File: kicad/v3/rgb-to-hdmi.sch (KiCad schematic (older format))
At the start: 26 parts, among them P1 CONN_02X20, P2 CONN_01X03, P3 CONN_01X06, P4 CONN_01X02, P5 CONN_01X06, P6 CONN_01X02, P7 Conn_01x01, SW1 SW_PUSH, SW2 SW_PUSH, SW3 SW_PUSH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

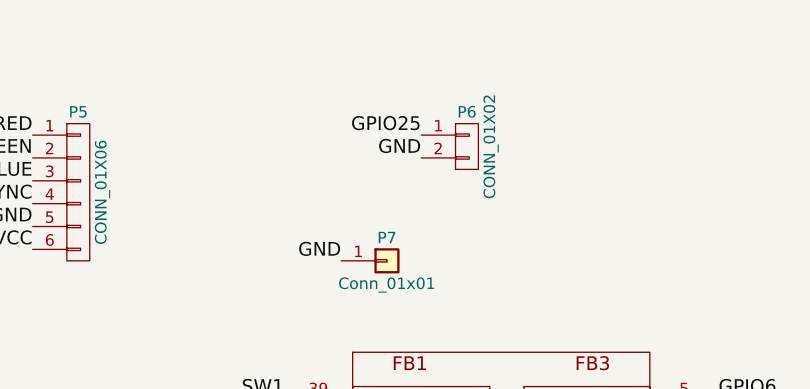
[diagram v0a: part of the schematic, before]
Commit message: KiCad: corrected via size, cleaned up silk screen
Change-Id: Icce07a46245585d3c723be4bf0025df466743eb7
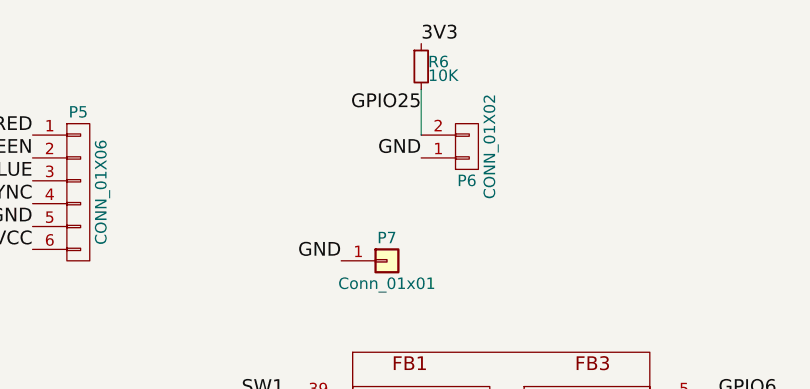
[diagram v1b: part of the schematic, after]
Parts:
- added R6: 10K, Resistors_SMD:R_0805_HandSoldering, symbol R_Small
- P6: footprint Pin_Headers:Pin_Header_Straight_1x02_Pitch2.54mm -> Pin_Headers:Pin_Header_Angled_1x02_Pitch2.54mm
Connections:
- net 3V3: now also R6.1
- net GND: now also P6.1 (P1); no longer P6.2 (P2)
- net GPIO25: now also P6.2 (P2), R6.2; no longer P6.1 (P1)
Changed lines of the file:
@@
 F 0 "P6" H 5600 1350 50  0000 C CNN
 F 1 "CONN_01X02" V 5700 1200 50  0000 C CNN
-F 2 "Pin_Headers:Pin_Header_Straight_1x02_Pitch2.54mm" H 5600 1200 50  0001 C CNN
+F 2 "Pin_Headers:Pin_Header_Angled_1x02_Pitch2.54mm" H 5600 1200 50  0001 C CNN
 F 3 "" H 5600 1200 50  0000 C CNN
 	1    5600 1200
-	1    0    0    -1
+	1    0    0    1
 $EndComp
 Text Label 5400 1250 2    60   ~ 0
 GND
-Text Label 5400 1150 2    60   ~ 0
+Text Label 5400 1050 2    60   ~ 0
 GPIO25
 Text Label 8950 2150 0    60   ~ 0
@@
 Text Label 5050 1700 2    60   ~ 0
 GND
+$Comp
+L R_Small R6
+U 1 1 5B1681C6
+P 5400 850
+F 0 "R6" H 5430 870 50  0000 L CNN
+F 1 "10K" H 5430 810 50  0000 L CNN
+F 2 "Resistors_SMD:R_0805_HandSoldering" H 5400 850 50  0001 C CNN
+F 3 "" H 5400 850 50  0000 C CNN
+	1    5400 850
+	1    0    0    -1
+$EndComp
+Wire Wire Line
+	5400 1150 5400 950
+Text Label 5400 750  0    60   ~ 0
+3V3
 $EndSCHEMATC

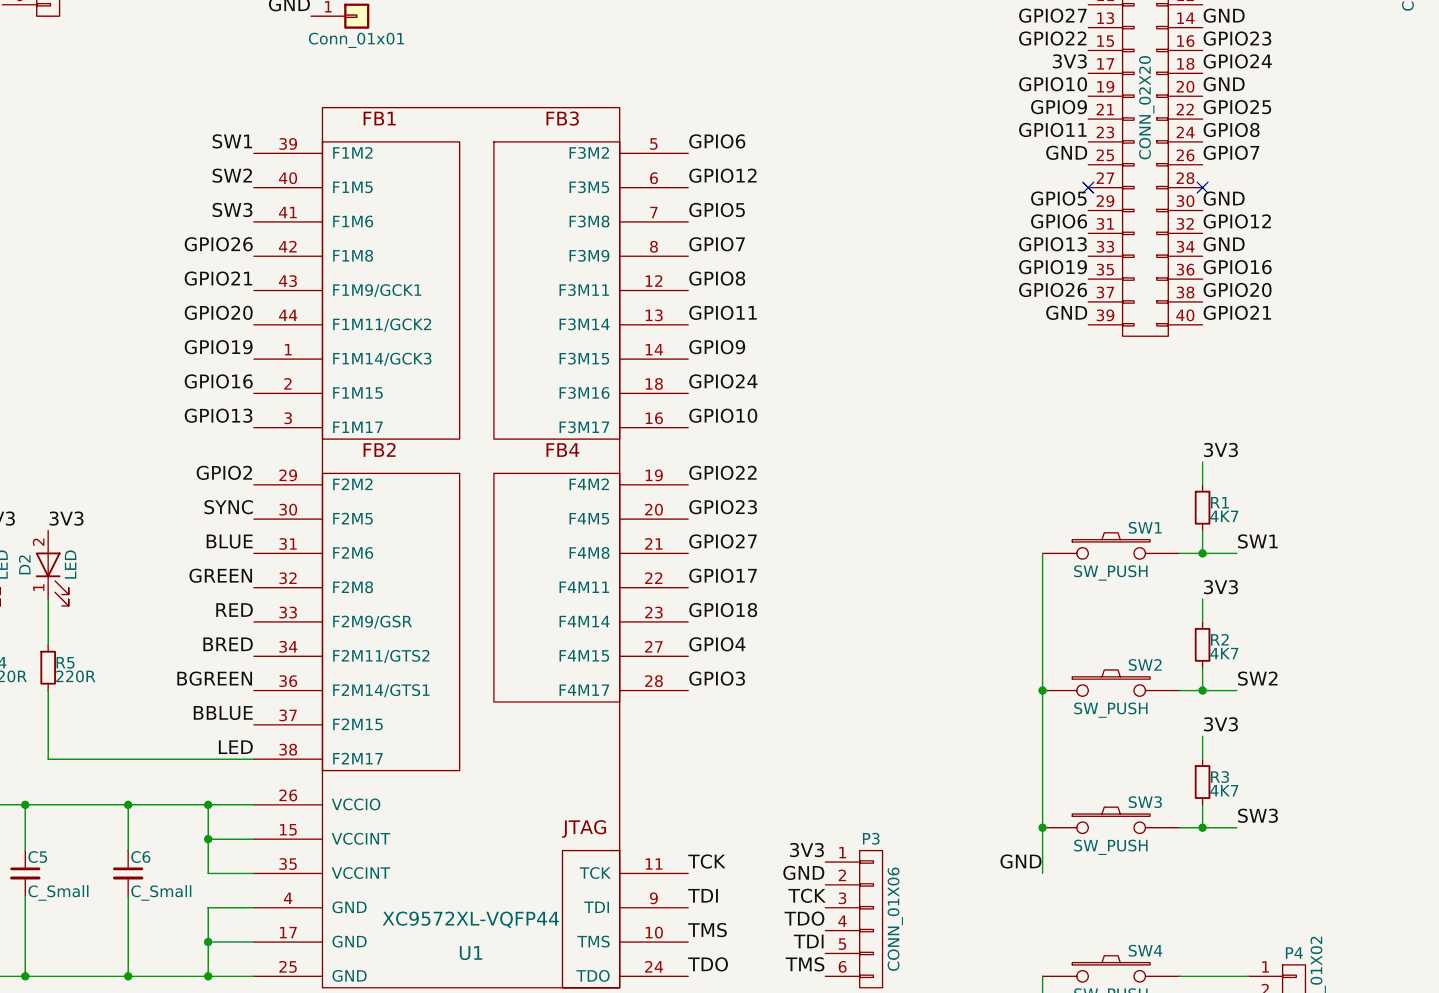
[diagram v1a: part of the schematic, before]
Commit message: KiCad: removed SW2/3 passthrough, use gpio 19/26 instead
Change-Id: I88240f36d608d24969d40a8aa7c47a878a85b3d9
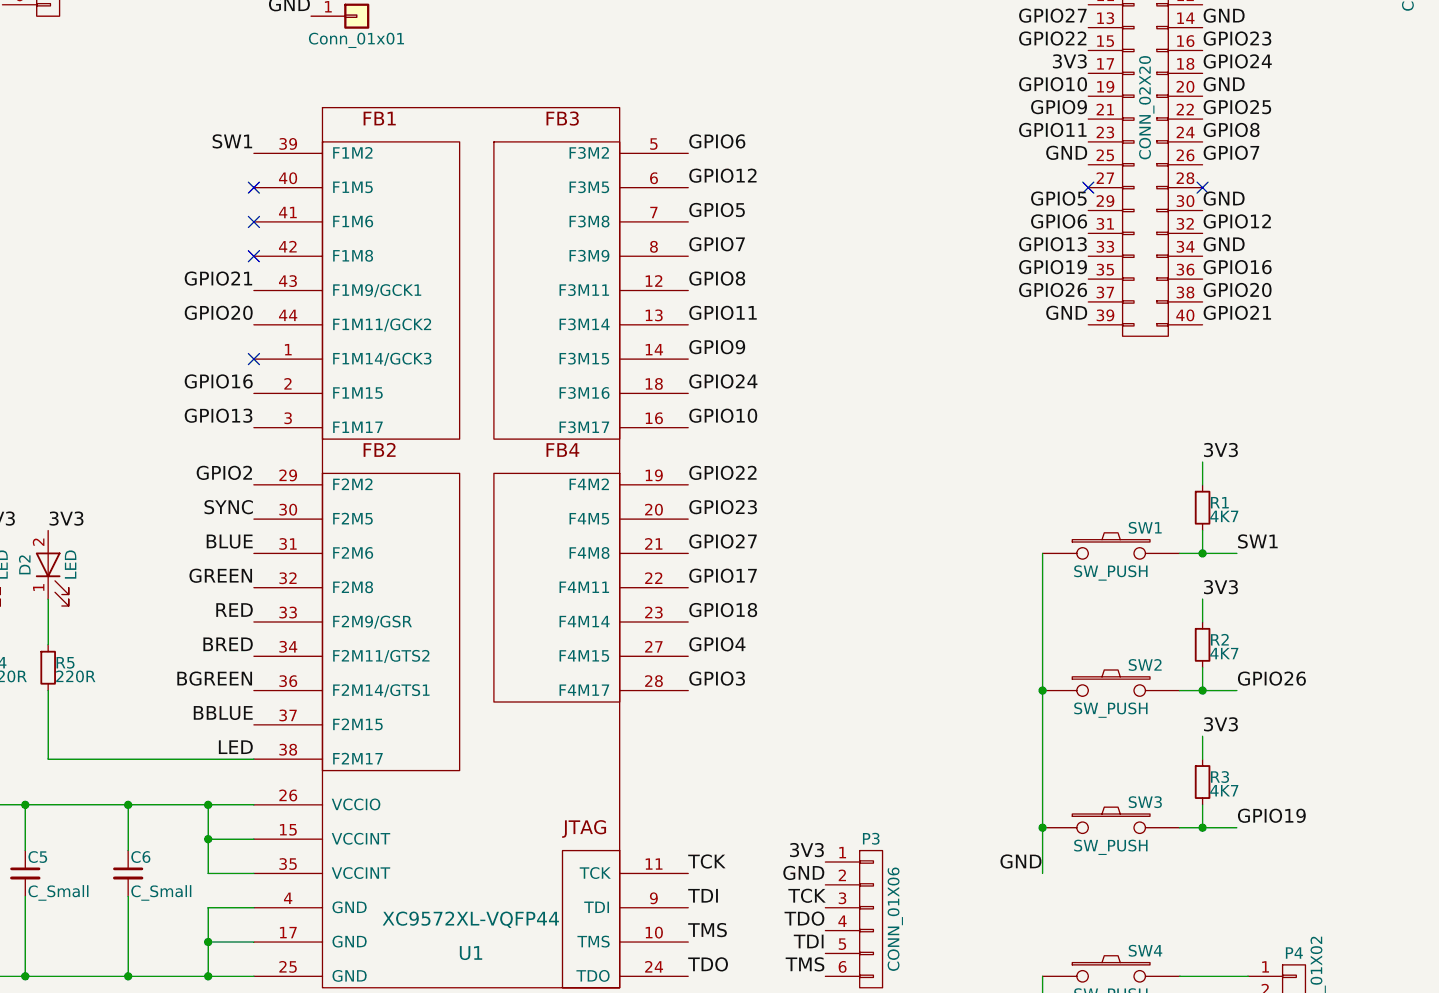
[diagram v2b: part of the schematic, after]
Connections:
- net GPIO19: now also R3.2, SW3.2; no longer U1.1 (F1M14/GCK3)
- net GPIO26: now also R2.2, SW2.2; no longer U1.42 (F1M8)
- removed net SW2: R2.2, SW2.2, U1.40 (F1M5)
- removed net SW3: R3.2, SW3.2, U1.41 (F1M6)
- no-connect marks 4 -> 8
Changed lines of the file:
@@
 Text Label 4800 3350 2    60   ~ 0
 GPIO16
-Text Label 4800 3200 2    60   ~ 0
-GPIO19
 Text Label 4800 2900 2    60   ~ 0
 GPIO21
 Text Label 4800 3050 2    60   ~ 0
 GPIO20
-Text Label 4800 2750 2    60   ~ 0
-GPIO26
 Text Label 4800 3900 2    60   ~ 0
 SYNC
@@
 	1    0    0    -1
 $EndComp
-Text Label 9100 4650 0    60   ~ 0
-SW2
-Text Label 9100 5250 0    60   ~ 0
-SW3
 Text Label 8950 4250 0    60   ~ 0
 3V3
@@
 	1    0    0    -1
 $EndComp
-Text Label 4800 2600 2    60   ~ 0
-SW3
-Text Label 4800 2450 2    60   ~ 0
-SW2
 Text Label 4800 4500 2    60   ~ 0
 BRED
@@
 Text Label 5400 750  0    60   ~ 0
 3V3
+NoConn ~ 4800 2450
+NoConn ~ 4800 2600
+Text Label 9100 4650 0    60   ~ 0
+GPIO26
+Text Label 9100 5250 0    60   ~ 0
+GPIO19
+NoConn ~ 4800 2750
+NoConn ~ 4800 3200
 $EndSCHEMATC

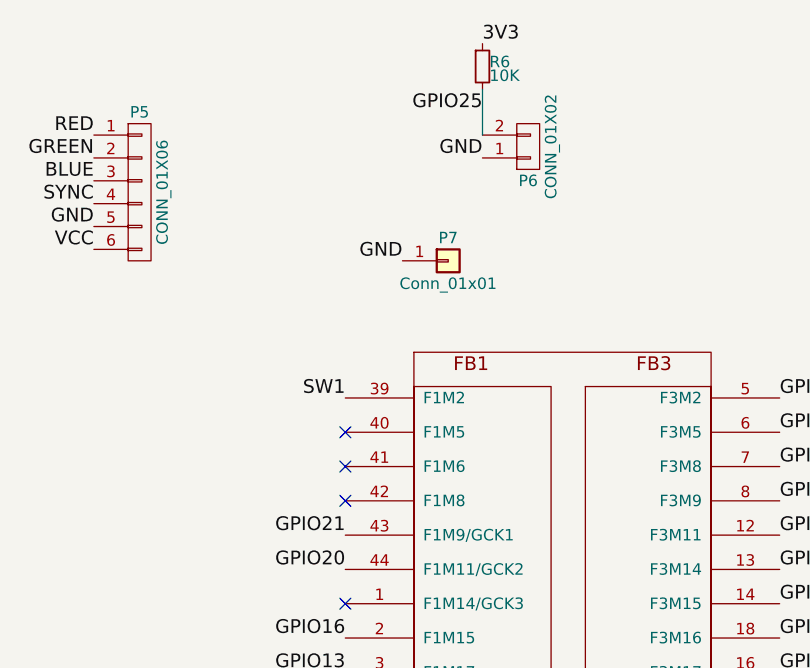
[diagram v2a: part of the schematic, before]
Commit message: KiCad and CPLD: final small changes to bring SW2/3/link inputs and LED1 output to CPLD (unused)
Change-Id: I054dcab88885547d6ceb07bc2759daf81372ef52
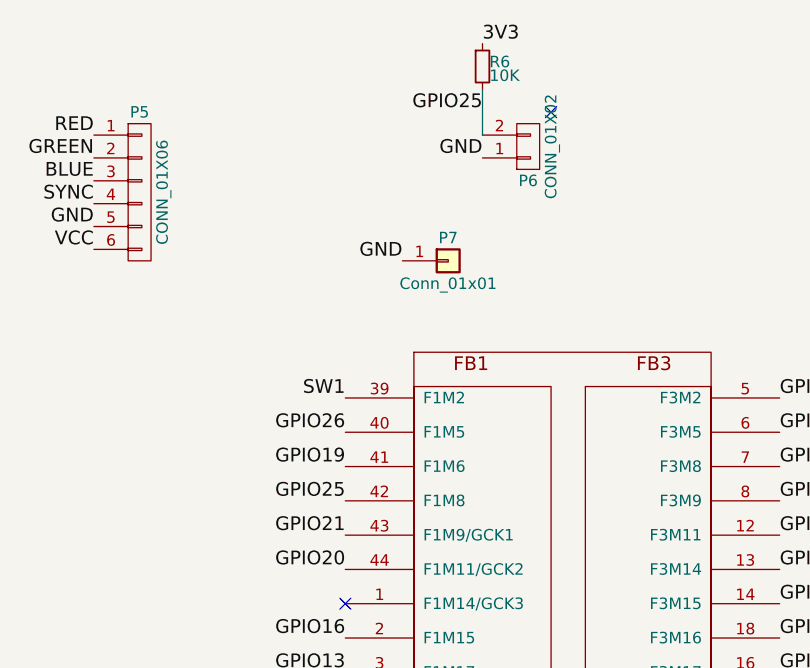
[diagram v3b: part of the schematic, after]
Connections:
- net GPIO19: now also U1.41 (F1M6)
- net GPIO25: now also U1.42 (F1M8)
- net GPIO26: now also U1.40 (F1M5)
- no-connect marks 8 -> 6
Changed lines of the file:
@@
 Text Label 5400 750  0    60   ~ 0
 3V3
-NoConn ~ 4800 2450
-NoConn ~ 4800 2600
 Text Label 9100 4650 0    60   ~ 0
 GPIO26
 Text Label 9100 5250 0    60   ~ 0
 GPIO19
-NoConn ~ 4800 2750
 NoConn ~ 4800 3200
+NoConn ~ 5700 1050
+Text Label 4800 2450 2    60   ~ 0
+GPIO26
+Text Label 4800 2600 2    60   ~ 0
+GPIO19
+Text Label 4800 2750 2    60   ~ 0
+GPIO25
 $EndSCHEMATC

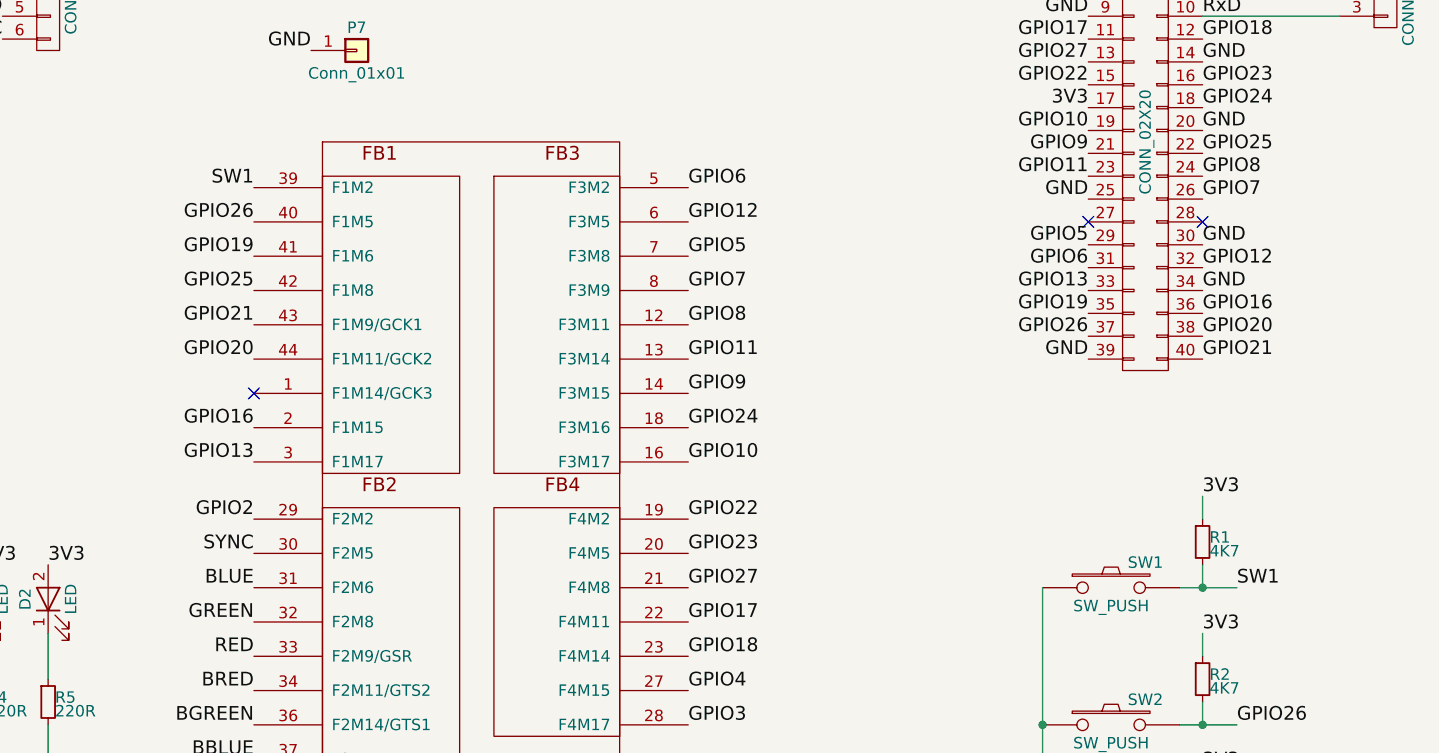
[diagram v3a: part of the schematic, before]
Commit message: KiCad: Removed SW1Out passthrough to save a produce term
Change-Id: I7cc547a21f411a16182b2e27dbd37bbfed956f1c
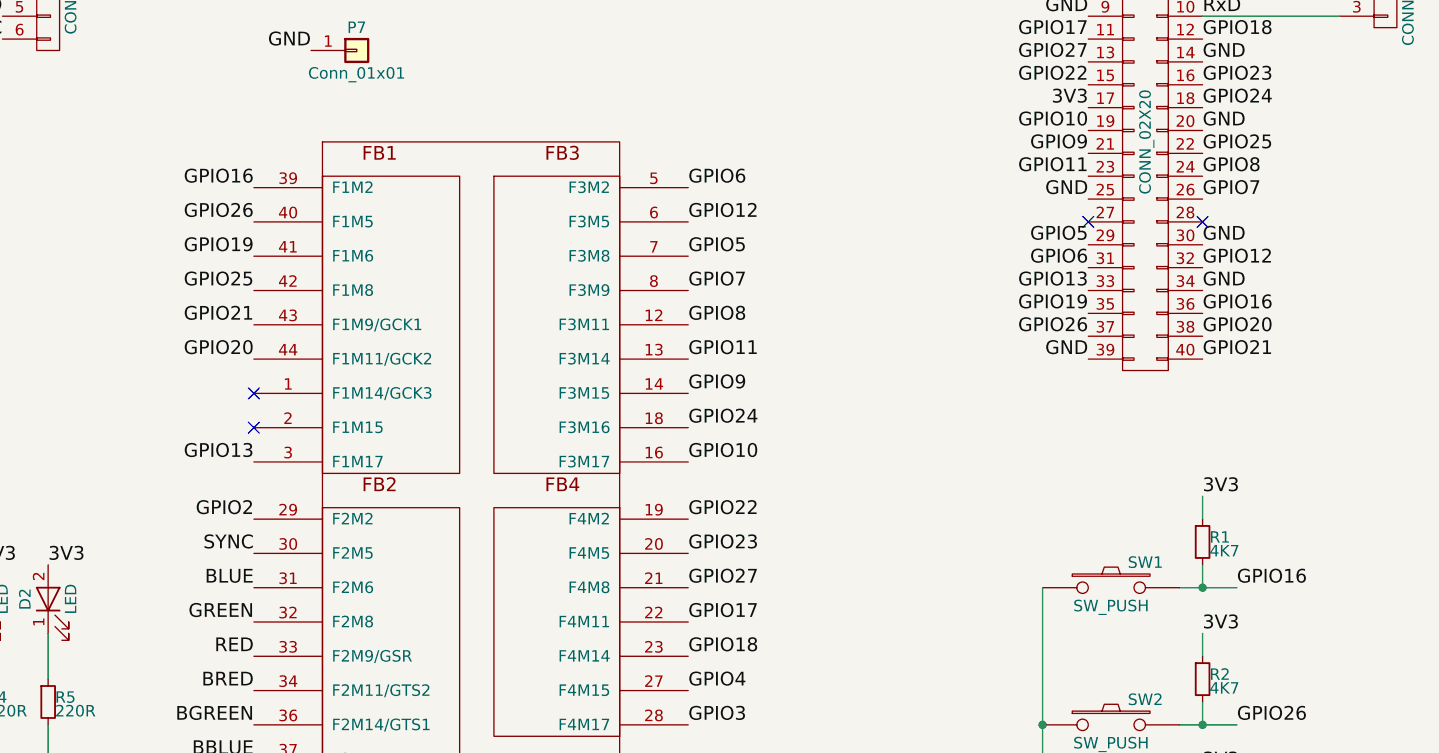
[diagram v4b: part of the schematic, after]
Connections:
- net SW1 is gone; now on net GPIO16: R1.2, SW1.2, U1.39 (F1M2)
- net GPIO16: no longer U1.2 (F1M15)
- no-connect marks 6 -> 7
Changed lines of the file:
@@
 Text Label 4800 3500 2    60   ~ 0
 GPIO13
-Text Label 4800 3350 2    60   ~ 0
-GPIO16
 Text Label 4800 2900 2    60   ~ 0
 GPIO21
@@
 3V3
 Text Label 9100 4050 0    60   ~ 0
-SW1
+GPIO16
 $Comp
 L SW_PUSH SW2
@@
 $EndComp
 Text Label 4800 2300 2    60   ~ 0
-SW1
+GPIO16
 Text Label 8450 1750 2    60   ~ 0
 GPIO27
@@
 Text Label 4800 2750 2    60   ~ 0
 GPIO25
+NoConn ~ 4800 3350
 $EndSCHEMATC
